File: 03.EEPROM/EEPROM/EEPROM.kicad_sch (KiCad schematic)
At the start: 0 parts

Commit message: EEPROM - EESCHEMA - SYMBOL
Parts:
- added BT1: Battery, symbol Device:Battery
- added C1, C2, C3, C4: C, symbol Device:C
- added C5: C_Polarized, symbol Device:C_Polarized
- added D1, D2: LED, symbol Device:LED
- added H1, H2, H3, H4: MountingHole, symbol Mechanical:MountingHole
- added R1, R2, R3, R4, R5, R6, R7: R, symbol Device:R
- added U1, U2: 24LC1025, symbol Memory_EEPROM:24LC1025
- added U3: DS1337S_, DS1337S_:SOIC127P600X175-8N, symbol DS1337S_:DS1337S_
- added U4: ATMEGA328P-AU, ATMEGA328P-AU:QFP80P900X900X120-32N, symbol ATMEGA328P-AU:ATMEGA328P-AU
- added Y1, Y2: Crystal, symbol Device:Crystal
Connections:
- new net: U4.21 (GND), U4.3 (GND), U4.5 (GND)
- new net: U4.4 (VCC), U4.6 (VCC)

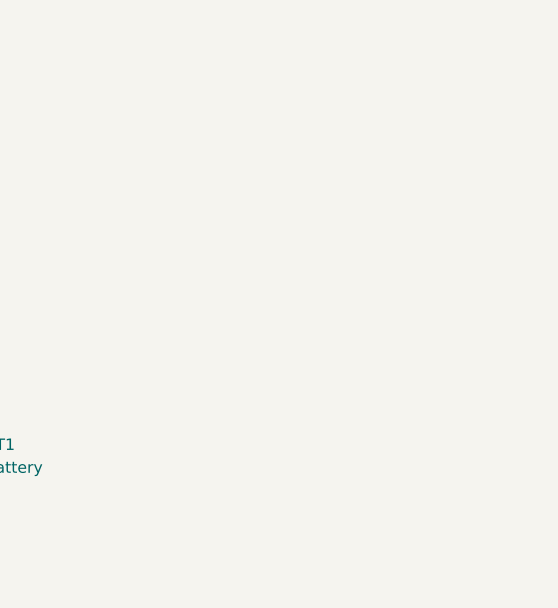
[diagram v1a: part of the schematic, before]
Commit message: EEPROM - EESCHEMA - SYMBOL 2 SHEET
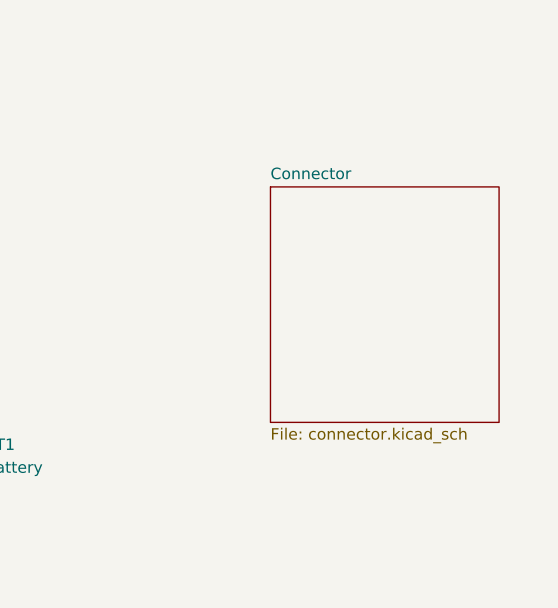
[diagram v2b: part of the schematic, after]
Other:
- added sheet Connector (connector.kicad_sch)
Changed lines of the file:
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@@
+		)
+	)
+	(sheet
+		(at 203.2 76.2)
+		(size 25.4 26.162)
+		(exclude_from_sim no)
+		(in_bom yes)
+		(on_board yes)
+		(dnp no)
+		(fields_autoplaced yes)
+		(stroke
+			(width 0.1524)
+			(type solid)
+		)
+		(fill
+			(color 0 0 0 0.0000)
+		)
+		(property "Sheetname" "Connector"
+			(at 203.2 75.4884 0)
+			(effects
+				(font
+					(size 1.27 1.27)
+				)
+				(justify left bottom)
+			)
+		)
+		(property "Sheetfile" "connector.kicad_sch"
+			(at 203.2 102.9466 0)
+			(effects
+				(font
+					(size 1.27 1.27)
+				)
+				(justify left top)
+			)
+		)
+		(instances
+			(project "EEPROM"
+				(path "/b4f5f33e-7286-44f8-9677-0db3208b5bbd"
+					(page "2")
+				)
+			)
 		)
 	)

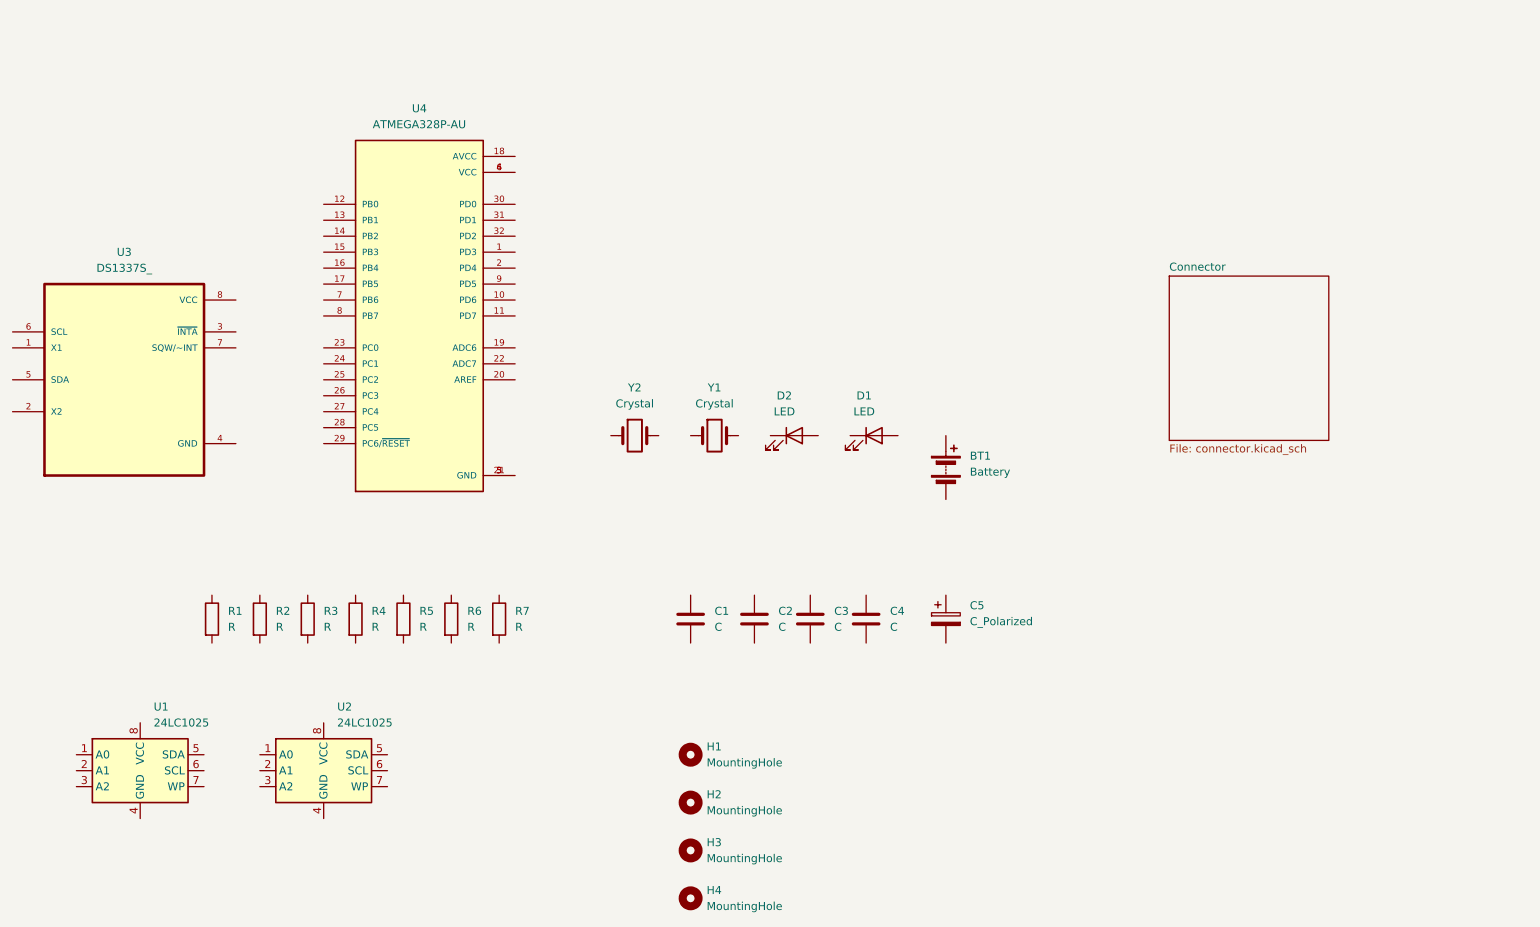
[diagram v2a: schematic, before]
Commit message: EEPROM - EESCHEMA - ARRANGE, ANNOTATE
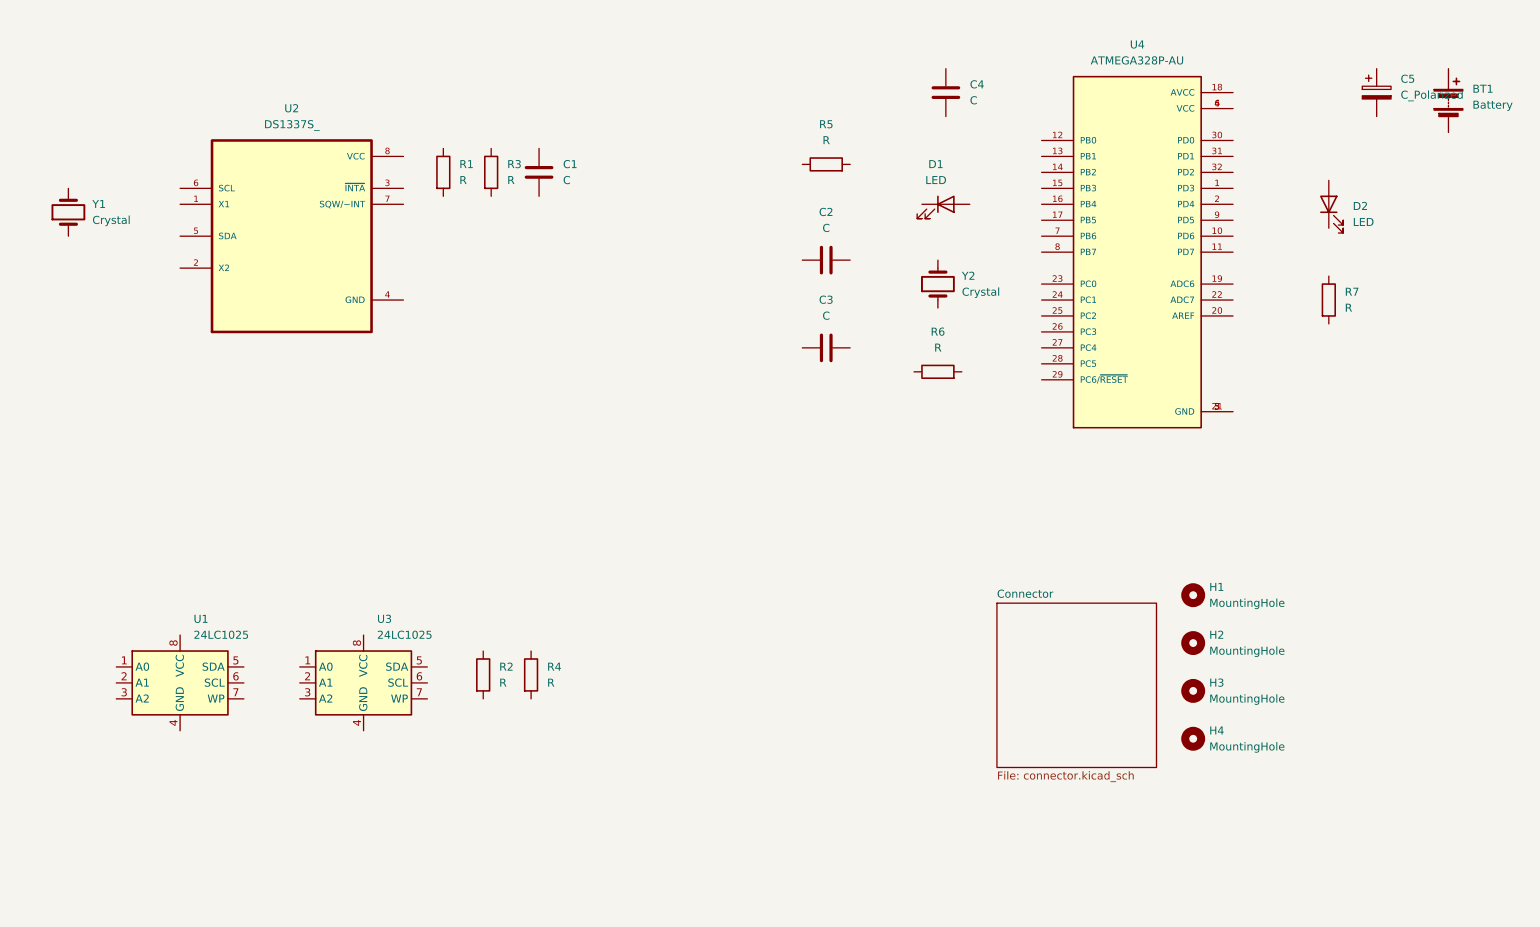
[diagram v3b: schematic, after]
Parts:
- renumbered C3 to C2, C2 to C3, R5 to R1, R1 to R2, R4 to R3, R2 to R4, R6 to R5, R7 to R6, R3 to R7, U3 to U2, U2 to U3, Y2 to Y1, Y1 to Y2
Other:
- moved on the sheet: BT1, C1, C2, C3, C4, C5, D1, D2, H1, H2, H3, H4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

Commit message: EEPROM - EESCHEMA - EDIT COMPONENT
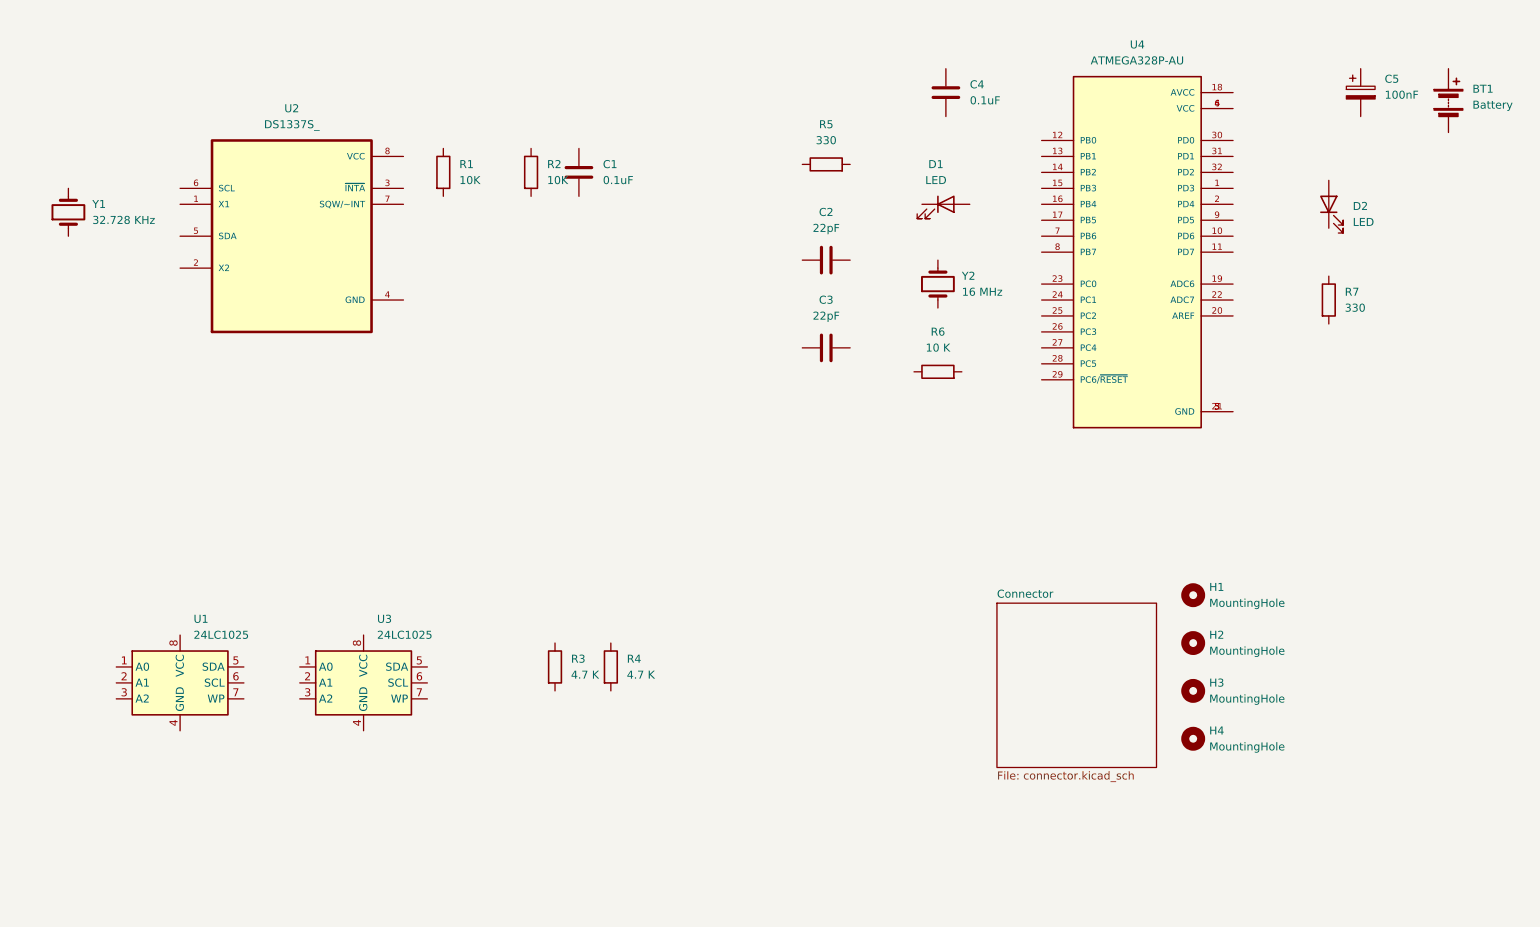
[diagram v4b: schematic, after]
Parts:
- C1, C4: value C -> 0.1uF
- C2, C3: value C -> 22pF
- C5: value C_Polarized -> 100nF
- R1: value R -> 10K
- R2: renamed from R3; value R -> 10K
- R3: renamed from R2; value R -> 4.7 K
- R4: value R -> 4.7 K
- R5, R7: value R -> 330
- R6: value R -> 10 K
- Y1: value Crystal -> 32.728 KHz
- Y2: value Crystal -> 16 MHz
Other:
- moved on the sheet: C1, C5, R2, R3, R4
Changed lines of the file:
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@@
 			)
 		)
-		(property "Value" "R"
+		(property "Value" "330"
 			(at 148.59 54.61 90)
 			(effects
@@
 	(symbol
 		(lib_id "Device:C")
-		(at 102.87 59.69 0)
+		(at 109.22 59.69 0)
 		(unit 1)
 		(exclude_from_sim no)
@@
 		(fields_autoplaced yes)
 		(property "Reference" "C1"
-			(at 106.68 58.4199 0)
-			(effects
-				(font
-					(size 1.27 1.27)
-				)
-				(justify left)
-			)
-		)
-		(property "Value" "C"
-			(at 106.68 60.9599 0)
-			(effects
-				(font
-					(size 1.27 1.27)
-				)
-				(justify left)
-			)
-		)
-		(property "Footprint" ""
-			(at 103.8352 63.5 0)
-			(effects
-				(font
-					(size 1.27 1.27)
-				)
-				(hide yes)
-			)
-		)
-		(property "Datasheet" "~"
-			(at 102.87 59.69 0)
+			(at 113.03 58.4199 0)
+			(effects
+				(font
+					(size 1.27 1.27)
+				)
+				(justify left)
+			)
+		)
+		(property "Value" "0.1uF"
+			(at 113.03 60.9599 0)
+			(effects
+				(font
+					(size 1.27 1.27)
+				)
+				(justify left)
+			)
+		)
+		(property "Footprint" ""
+			(at 110.1852 63.5 0)
+			(effects
+				(font
+					(size 1.27 1.27)
+				)
+				(hide yes)
+			)
+		)
+		(property "Datasheet" "~"
+			(at 109.22 59.69 0)
 			(effects
 				(font
@@
 		)
 		(property "Description" "Unpolarized capacitor"
-			(at 102.87 59.69 0)
+			(at 109.22 59.69 0)
 			(effects
 				(font
@@
 	(symbol
 		(lib_id "Device:R")
-		(at 101.6 139.7 0)
+		(at 114.3 138.43 0)
 		(unit 1)
 		(exclude_from_sim no)
@@
 		(fields_autoplaced yes)
 		(property "Reference" "R4"
-			(at 104.14 138.4299 0)
-			(effects
-				(font
-					(size 1.27 1.27)
-				)
-				(justify left)
-			)
-		)
-		(property "Value" "R"
-			(at 104.14 140.9699 0)
-			(effects
-				(font
-					(size 1.27 1.27)
-				)
-				(justify left)
-			)
-		)
-		(property "Footprint" ""
-			(at 99.822 139.7 90)
-			(effects
-				(font
-					(size 1.27 1.27)
-				)
-				(hide yes)
-			)
-		)
-		(property "Datasheet" "~"
-			(at 101.6 139.7 0)
+			(at 116.84 137.1599 0)
+			(effects
+				(font
+					(size 1.27 1.27)
+				)
+				(justify left)
+			)
+		)
+		(property "Value" "4.7 K"
+			(at 116.84 139.6999 0)
+			(effects
+				(font
+					(size 1.27 1.27)
+				)
+				(justify left)
+			)
+		)
+		(property "Footprint" ""
+			(at 112.522 138.43 90)
+			(effects
+				(font
+					(size 1.27 1.27)
+				)
+				(hide yes)
+			)
+		)
+		(property "Datasheet" "~"
+			(at 114.3 138.43 0)
 			(effects
 				(font
@@
 		)
 		(property "Description" "Resistor"
-			(at 101.6 139.7 0)
+			(at 114.3 138.43 0)
 			(effects
 				(font
@@
 			)
 		)
-		(property "Value" "R"
+		(property "Value" "10K"
 			(at 90.17 60.9599 0)
 			(effects
@@
 			)
 		)
-		(property "Value" "R"
+		(property "Value" "330"
 			(at 231.14 81.2799 0)
 			(effects
@@
 			)
 		)
-		(property "Value" "R"
+		(property "Value" "10 K"
 			(at 166.37 87.63 90)
 			(effects
@@
 			)
 		)
-		(property "Value" "C"
+		(property "Value" "22pF"
 			(at 148.59 82.55 90)
 			(effects
@@
 			)
 		)
-		(property "Value" "C"
+		(property "Value" "22pF"
 			(at 148.59 68.58 90)
 			(effects
@@
 			)
 		)
-		(property "Value" "Crystal"
+		(property "Value" "32.728 KHz"
 			(at 31.75 67.3099 90)
 			(effects
@@
 	(symbol
 		(lib_id "Device:R")
-		(at 93.98 139.7 0)
+		(at 105.41 138.43 0)
 		(unit 1)
 		(exclude_from_sim no)
@@
 		(dnp no)
 		(fields_autoplaced yes)
-		(property "Reference" "R2"
-			(at 96.52 138.4299 0)
-			(effects
-				(font
-					(size 1.27 1.27)
-				)
-				(justify left)
-			)
-		)
-		(property "Value" "R"
-			(at 96.52 140.9699 0)
-			(effects
-				(font
-					(size 1.27 1.27)
-				)
-				(justify left)
-			)
-		)
-		(property "Footprint" ""
-			(at 92.202 139.7 90)
-			(effects
-				(font
-					(size 1.27 1.27)
-				)
-				(hide yes)
-			)
-		)
-		(property "Datasheet" "~"
-			(at 93.98 139.7 0)
+		(property "Reference" "R3"
+			(at 107.95 137.1599 0)
+			(effects
+				(font
+					(size 1.27 1.27)
+				)
+				(justify left)
+			)
+		)
+		(property "Value" "4.7 K"
+			(at 107.95 139.6999 0)
+			(effects
+				(font
+					(size 1.27 1.27)
+				)
+				(justify left)
+			)
+		)
+		(property "Footprint" ""
+			(at 103.632 138.43 90)
+			(effects
+				(font
+					(size 1.27 1.27)
+				)
+				(hide yes)
+			)
+		)
+		(property "Datasheet" "~"
+			(at 105.41 138.43 0)
 			(effects
 				(font
@@
 		)
 		(property "Description" "Resistor"
-			(at 93.98 139.7 0)
+			(at 105.41 138.43 0)
 			(effects
 				(font
@@
 			(project ""
 				(path "/b4f5f33e-7286-44f8-9677-0db3208b5bbd"
-					(reference "R2")
+					(reference "R3")
 					(unit 1)
 				)
@@
 			)
 		)
-		(property "Value" "C"
+		(property "Value" "0.1uF"
 			(at 171.45 48.2599 0)
 			(effects
@@
 	(symbol
 		(lib_id "Device:R")
-		(at 95.25 59.69 0)
+		(at 101.6 59.69 0)
 		(unit 1)
 		(exclude_from_sim no)
@@
 		(dnp no)
 		(fields_autoplaced yes)
-		(property "Reference" "R3"
-			(at 97.79 58.4199 0)
-			(effects
-				(font
-					(size 1.27 1.27)
-				)
-				(justify left)
-			)
-		)
-		(property "Value" "R"
-			(at 97.79 60.9599 0)
-			(effects
-				(font
-					(size 1.27 1.27)
-				)
-				(justify left)
-			)
-		)
-		(property "Footprint" ""
-			(at 93.472 59.69 90)
-			(effects
-				(font
-					(size 1.27 1.27)
-				)
-				(hide yes)
-			)
-		)
-		(property "Datasheet" "~"
-			(at 95.25 59.69 0)
+		(property "Reference" "R2"
+			(at 104.14 58.4199 0)
+			(effects
+				(font
+					(size 1.27 1.27)
+				)
+				(justify left)
+			)
+		)
+		(property "Value" "10K"
+			(at 104.14 60.9599 0)
+			(effects
+				(font
+					(size 1.27 1.27)
+				)
+				(justify left)
+			)
+		)
+		(property "Footprint" ""
+			(at 99.822 59.69 90)
+			(effects
+				(font
+					(size 1.27 1.27)
+				)
+				(hide yes)
+			)
+		)
+		(property "Datasheet" "~"
+			(at 101.6 59.69 0)
 			(effects
 				(font
@@
 		)
 		(property "Description" "Resistor"
-			(at 95.25 59.69 0)
+			(at 101.6 59.69 0)
 			(effects
 				(font
@@
 			(project "EEPROM"
 				(path "/b4f5f33e-7286-44f8-9677-0db3208b5bbd"
-					(reference "R3")
+					(reference "R2")
 					(unit 1)
 				)
@@
 			)
 		)
-		(property "Value" "Crystal"
+		(property "Value" "16 MHz"
 			(at 170.18 78.7399 90)
 			(effects
@@
 	(symbol
 		(lib_id "Device:C_Polarized")
-		(at 236.22 46.99 0)
+		(at 233.68 46.99 0)
 		(unit 1)
 		(exclude_from_sim no)
@@
 		(fields_autoplaced yes)
 		(property "Reference" "C5"
-			(at 240.03 44.8309 0)
-			(effects
-				(font
-					(size 1.27 1.27)
-				)
-				(justify left)
-			)
-		)
-		(property "Value" "C_Polarized"
-			(at 240.03 47.3709 0)
-			(effects
-				(font
-					(size 1.27 1.27)
-				)
-				(justify left)
-			)
-		)
-		(property "Footprint" ""
-			(at 237.1852 50.8 0)
-			(effects
-				(font
-					(size 1.27 1.27)
-				)
-				(hide yes)
-			)
-		)
-		(property "Datasheet" "~"
-			(at 236.22 46.99 0)
+			(at 237.49 44.8309 0)
+			(effects
+				(font
+					(size 1.27 1.27)
+				)
+				(justify left)
+			)
+		)
+		(property "Value" "100nF"
+			(at 237.49 47.3709 0)
+			(effects
+				(font
+					(size 1.27 1.27)
+				)
+				(justify left)
+			)
+		)
+		(property "Footprint" ""
+			(at 234.6452 50.8 0)
+			(effects
+				(font
+					(size 1.27 1.27)
+				)
+				(hide yes)
+			)
+		)
+		(property "Datasheet" "~"
+			(at 233.68 46.99 0)
 			(effects
 				(font
@@
 		)
 		(property "Description" "Polarized capacitor"
-			(at 236.22 46.99 0)
-			(effects
-				(font
+			(at 233.68 46.99 0)
+			(effects
+				(font
